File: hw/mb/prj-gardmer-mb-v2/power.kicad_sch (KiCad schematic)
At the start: 5 parts, among them SW11 ON_OFF_SW

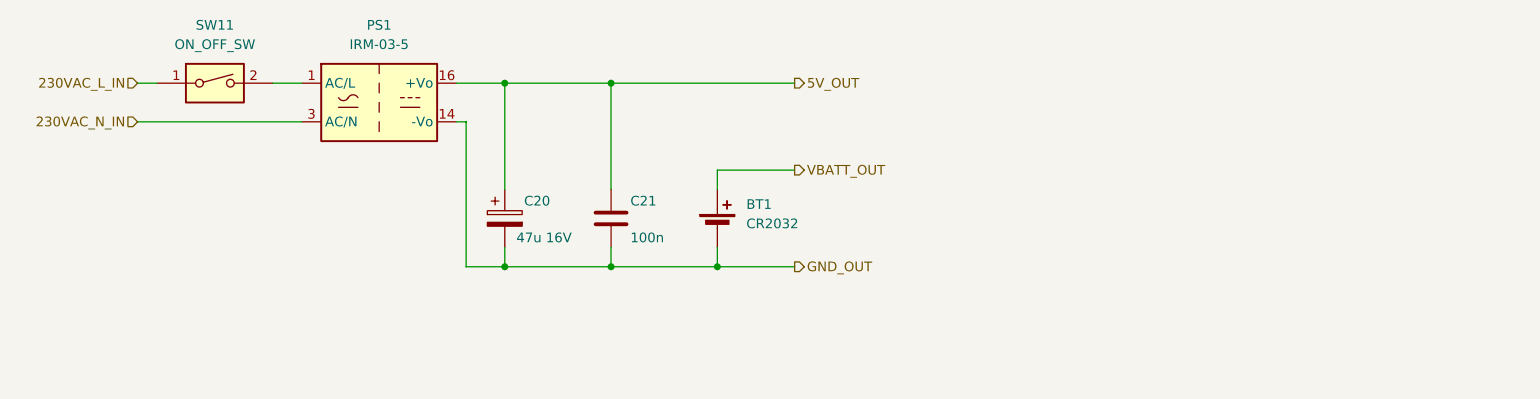
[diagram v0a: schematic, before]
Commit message: Added footprints and bom. Updated schematics.
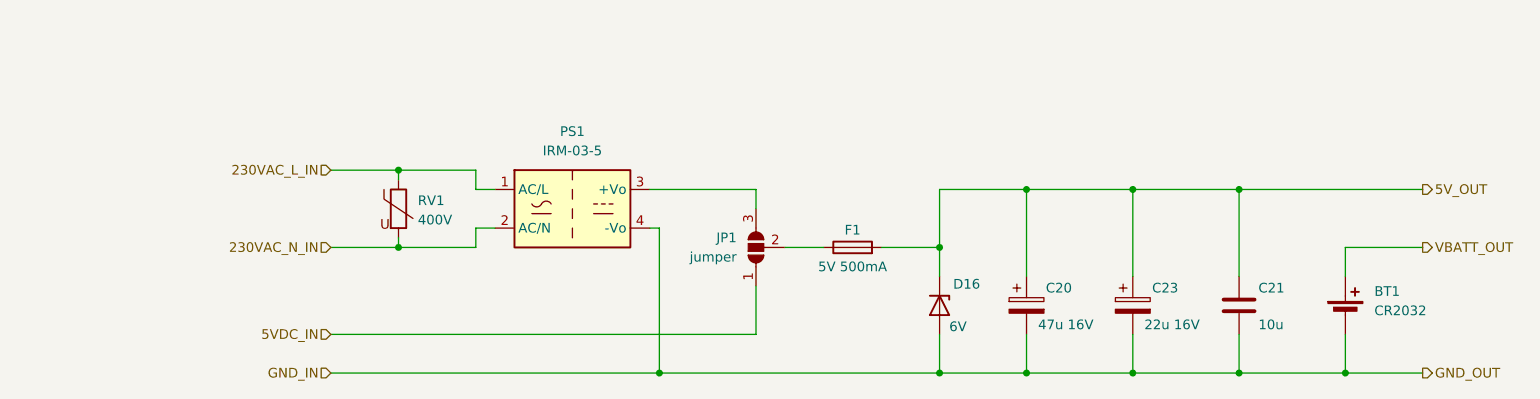
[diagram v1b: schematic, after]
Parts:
- removed SW11: ON_OFF_SW, symbol alf64:SW_DIP_x01
- added C23: 22u 16V, symbol alf64:C_Polarized
- added D16: 6V, symbol alf64:D_Zener
- added F1: 5V 500mA, symbol alf64:Fuse
- added JP1: jumper, symbol alf64:SolderJumper_3_Open
- added RV1: 400V, symbol alf64:Varistor
- C21: value 100n -> 10u
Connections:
- net 230VAC_L_IN: now also PS1.1 (AC/L), RV1.1
- net 230VAC_N_IN: now also PS1.2 (AC/N), RV1.2; no longer PS1.3 (AC/N)
- net 5V_OUT: now also C23.1, D16.1 (K), F1.2; no longer PS1.16 (+Vo)
- net GND_OUT renamed GND_IN
- net GND_IN: now also PS1.4 (-Vo), C23.2, D16.2 (A); no longer PS1.14 (-Vo)
- new net: F1.1, JP1.2 (C)
- new net: JP1.3 (B), PS1.3 (+Vo)
- new net 5VDC_IN: JP1.1 (A)
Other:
- moved on the sheet: BT1, C20, C21, PS1

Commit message: Assigned footprints to schematic symbols.
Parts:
- BT1: footprint (none) -> alf64:CR2032_Holder_DS1092
- C20, C23: footprint (none) -> alf64:C_Tantal_2312
- C21: footprint (none) -> alf64:Generic_0805
- D16: footprint (none) -> alf64:D_QuadroMelf
- F1: footprint (none) -> alf64:Generic_1206
- JP1: footprint (none) -> alf64:Solderjumper-3-rounded
- PS1: footprint Converter_ACDC:Converter_ACDC_MeanWell_IRM-03-xx_THT -> alf64:IRM-03
- RV1: footprint (none) -> alf64:RV_Disc_D21.5mm_W5.4mm_P10mm
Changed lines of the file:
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@@
 			)
 		)
-		(property "Footprint" ""
+		(property "Footprint" "alf64:Solderjumper-3-rounded"
 			(at 127 67.31 0)
 			(effects
@@
 			)
 		)
-		(property "Footprint" ""
+		(property "Footprint" "alf64:Generic_1206"
 			(at 139.7 69.088 90)
 			(effects
@@
 			)
 		)
-		(property "Footprint" ""
+		(property "Footprint" "alf64:CR2032_Holder_DS1092"
 			(at 204.47 74.676 90)
 			(effects
@@
 			)
 		)
-		(property "Footprint" ""
+		(property "Footprint" "alf64:C_Tantal_2312"
 			(at 177.4952 78.74 0)
 			(effects
@@
 			)
 		)
-		(property "Footprint" ""
+		(property "Footprint" "alf64:Generic_0805"
 			(at 191.4652 78.74 0)
 			(effects
@@
 			)
 		)
-		(property "Footprint" ""
+		(property "Footprint" "alf64:D_QuadroMelf"
 			(at 151.13 74.93 0)
 			(effects
@@
 			)
 		)
-		(property "Footprint" "Converter_ACDC:Converter_ACDC_MeanWell_IRM-03-xx_THT"
+		(property "Footprint" "alf64:IRM-03"
 			(at 102.87 71.12 0)
 			(effects
@@
 			)
 		)
-		(property "Footprint" ""
+		(property "Footprint" "alf64:RV_Disc_D21.5mm_W5.4mm_P10mm"
 			(at 78.232 62.23 90)
 			(effects
@@
 			)
 		)
-		(property "Footprint" ""
+		(property "Footprint" "alf64:C_Tantal_2312"
 			(at 163.5252 78.74 0)
 			(effects

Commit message: Updated schematic (footprints assign), PCB and footprints: - Changed the 'Generic' footprints that were used for capacitors, resistors and fuses into specific ones (I.e. Generic_0805 is replaced by C_0805 and R_0805). - Differentiated the D_0805 and LED_0805 footprints
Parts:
- C21: footprint alf64:Generic_0805 -> alf64:C_0805
- F1: footprint alf64:Generic_1206 -> alf64:Fuse_1206
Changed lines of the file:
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@@
 			)
 		)
-		(property "Footprint" "alf64:Generic_1206"
+		(property "Footprint" "alf64:Fuse_1206"
 			(at 139.7 69.088 90)
 			(effects
@@
 			)
 		)
-		(property "Footprint" "alf64:Generic_0805"
+		(property "Footprint" "alf64:C_0805"
 			(at 191.4652 78.74 0)
 			(effects

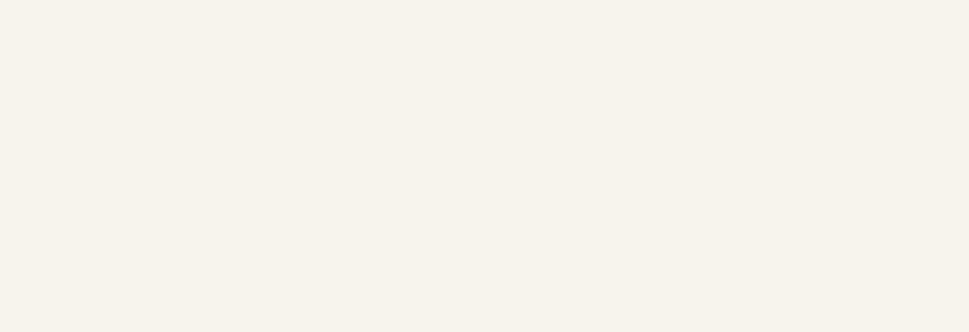
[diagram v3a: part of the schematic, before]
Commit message: Updated the hw release of prj-gardmer-mb-v2 rev001: - reorganized files in catalogues - added schematic in .pdf - added top & bottom elements on pcb in .pdf - added bom
Updated schematic:
- added a title, rev and date to the drawing info table on each sheet
- excluded test points ('TP' elements) from BOM

Updated PCB:
- added a title, rev and date to the drawing info table
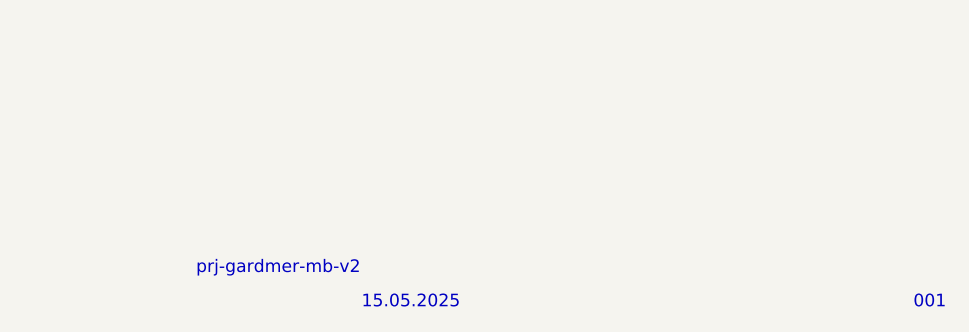
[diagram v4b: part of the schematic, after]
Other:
- note added: "001"
- note added: "15.05.2025"
- note added: "prj-gardmer-mb-v2"
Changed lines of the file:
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@@
+		)
+	)
+	(text "prj-gardmer-mb-v2"
+		(exclude_from_sim no)
+		(at 199.136 189.484 0)
+		(effects
+			(font
+				(size 1.397 1.397)
+			)
+		)
+	)
+	(text "15.05.2025"
+		(exclude_from_sim no)
+		(at 213.868 193.294 0)
+		(effects
+			(font
+				(size 1.397 1.397)
+			)
+		)
+	)
+	(text "001"
+		(exclude_from_sim no)
+		(at 271.526 193.294 0)
+		(effects
+			(font
+				(size 1.397 1.397)
+			)
 		)
 	)
